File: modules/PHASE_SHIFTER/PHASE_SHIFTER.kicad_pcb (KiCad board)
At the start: 2 copper layers, 160 x 100 mm, 2 parts, among them J1 Card_Connector

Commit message: started phase shifter
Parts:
- added C1: 470n, FormantKO:C_Rect, F.Cu at (123.2, 101.2)
- added C10: 10µ, FormantKO:CP_Axial_600, F.Cu at (182.0, 110.0)
- added C11: 10µ, FormantKO:CP_Axial_600, F.Cu at (182.0, 80.0)
- added C2: 4µ7, FormantKO:CP_Axial_600, F.Cu at (139.6, 121.7)
- added C3: 1µ, FormantKO:C_Rect, F.Cu at (123.2, 105.3)
- added C4: 470n, FormantKO:C_Rect, F.Cu at (123.2, 109.4)
- added C5: 330n, FormantKO:C_Rect, F.Cu at (123.2, 113.5)
- added C6: 150n, FormantKO:C_Rect, F.Cu at (123.2, 117.6)
- added C7: 100n, FormantKO:C_Rect, F.Cu at (123.2, 121.7)
- added C8: 47n, FormantKO:C_Rect, F.Cu at (123.2, 125.8)
- added D1: type="" model="12V" lib="semiconductor.lib", FormantKO:DUZ, F.Cu at (189.0, 111.9)
- added D2: 12V, FormantKO:DUZ, F.Cu at (189.0, 82.0)
- added IC1: LM324, FormantKO:DIP-14, F.Cu at (136.1, 108.8)
- added IC2: LM324, FormantKO:DIP-14, F.Cu at (147.7, 108.8)
- added P2: 50k, FormantKO:Potentiometer_Trimmer, F.Cu at (159.0, 120.3)
- added P4: 10k, FormantKO:PanelConnector_1x03, F.Cu at (159.5, 102.5)
- added R1: 100k, FormantKO:R_Axial_Horizontal, F.Cu at (126.5, 64.8)
- added R10: 22k, FormantKO:R_Axial_Horizontal, F.Cu at (142.3, 64.8)
- added R11: 22k, FormantKO:R_Axial_Horizontal, F.Cu at (142.3, 68.8)
- added R12: 22k, FormantKO:R_Axial_Horizontal, F.Cu at (142.3, 72.8)
- added R13: 22k, FormantKO:R_Axial_Horizontal, F.Cu at (142.3, 76.9)
- added R14: 22k, FormantKO:R_Axial_Horizontal, F.Cu at (142.3, 81.0)
- added R15: 100k, FormantKO:R_Axial_Horizontal, F.Cu at (142.3, 85.0)
- added R16: 100k, FormantKO:R_Axial_Horizontal, F.Cu at (142.3, 89.0)
- added R17: 100k, FormantKO:R_Axial_Horizontal, F.Cu at (142.3, 93.1)
- added R18: 100k, FormantKO:R_Axial_Horizontal, F.Cu at (142.3, 97.2)
- added R19: 100k, FormantKO:R_Axial_Horizontal, F.Cu at (158.1, 64.8)
- added R2: 100k, FormantKO:R_Axial_Horizontal, F.Cu at (126.5, 68.8)
- added R20: 100k, FormantKO:R_Axial_Horizontal, F.Cu at (158.1, 68.8)
- added R21: 22k, FormantKO:R_Axial_Horizontal, F.Cu at (158.1, 72.8)
- added R22: 22k, FormantKO:R_Axial_Horizontal, F.Cu at (158.1, 76.9)
- added R23: 10k, FormantKO:R_Axial_Horizontal, F.Cu at (158.1, 81.0)
- added R3: 22k, FormantKO:R_Axial_Horizontal, F.Cu at (126.5, 72.8)
- added R35: 10k, FormantKO:R_Axial_Horizontal, F.Cu at (158.1, 85.0)
- added R37: 150R, FormantKO:R_Axial_Horizontal, F.Cu at (195.0, 111.3)
- added R38: 150R, FormantKO:R_Axial_Horizontal, F.Cu at (195.0, 78.7)
- added R4: 22k, FormantKO:R_Axial_Horizontal, F.Cu at (126.5, 76.9)
- added R5: 22k, FormantKO:R_Axial_Horizontal, F.Cu at (126.5, 81.0)
- added R6: 22k, FormantKO:R_Axial_Horizontal, F.Cu at (126.5, 85.0)
- added R7: 22k, FormantKO:R_Axial_Horizontal, F.Cu at (126.5, 89.0)
- added R8: 22k, FormantKO:R_Axial_Horizontal, F.Cu at (126.5, 93.1)
- added R9: 22k, FormantKO:R_Axial_Horizontal, F.Cu at (126.5, 97.2)
- added S1: PHASING, FormantKO:PanelConnector_1x03, F.Cu at (159.5, 110.3)
- added T1: N-FET, FormantKO:TO-92, F.Cu at (112.0, 66.8)
- added T2: N-FET, FormantKO:TO-92, F.Cu at (112.0, 73.4)
- added T3: N-FET, FormantKO:TO-92, F.Cu at (112.0, 80.0)
- added T4: N-FET, FormantKO:TO-92, F.Cu at (112.0, 86.6)
- added T5: N-FET, FormantKO:TO-92, F.Cu at (112.0, 93.2)
- added T6: N-FET, FormantKO:TO-92, F.Cu at (112.0, 99.8)
- MH1: value ~ -> CardBracket; footprint FormantKO:Schroff_60807-011_3U_Pair -> FormantKO:Card_Bracket
- moved MH1 50.0 mm to (55.0, 95.0)
- moved J1 40.2 mm to (215.0, 95.0)

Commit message: not sure
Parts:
- moved P2 110.3 mm to (63.9, 64.5)
- moved S1 102.8 mm to (61.3, 79.8), turned to -90 degrees
- moved P4 98.2 mm to (61.3, 100.1), turned to -90 degrees
- moved R20 93.0 mm to (71.5, 102.6), turned to 90 degrees
- moved R22 84.7 mm to (74.0, 87.4)
- moved R23 84.5 mm to (74.0, 72.1), turned to 90 degrees
- moved R21 79.0 mm to (79.1, 72.1), turned to 90 degrees
- moved C2 76.5 mm to (74.0, 82.3)
- moved R35 74.8 mm to (96.9, 128.0), turned to 90 degrees
- moved T1 72.4 mm to (168.0, 112.8), turned to -90 degrees
- moved R14 66.3 mm to (81.7, 107.7)
- moved R13 65.9 mm to (81.7, 102.6)
- moved IC2 65.3 mm to (89.3, 79.8), turned to 180 degrees
- moved R19 61.5 mm to (104.5, 95.0)
- moved T2 60.4 mm to (157.9, 112.8), turned to -90 degrees
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
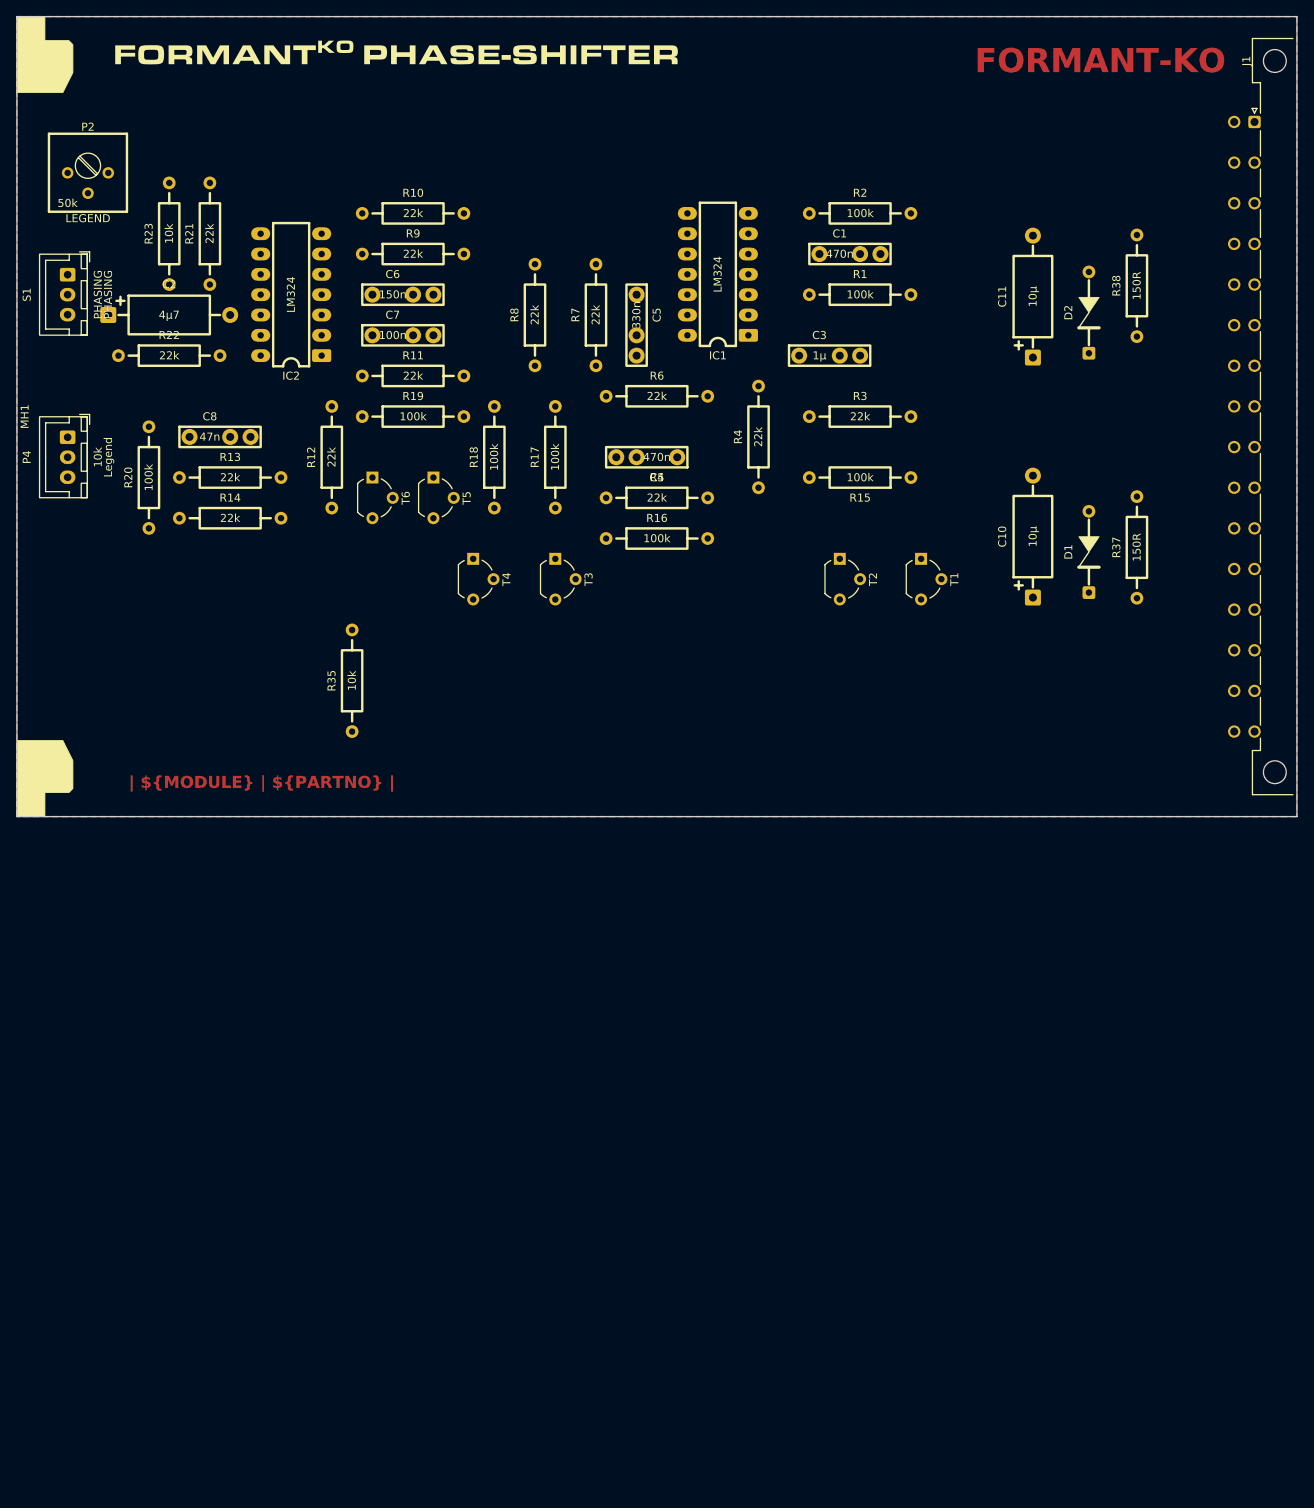
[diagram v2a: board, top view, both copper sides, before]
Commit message: phase shifter pcb placement
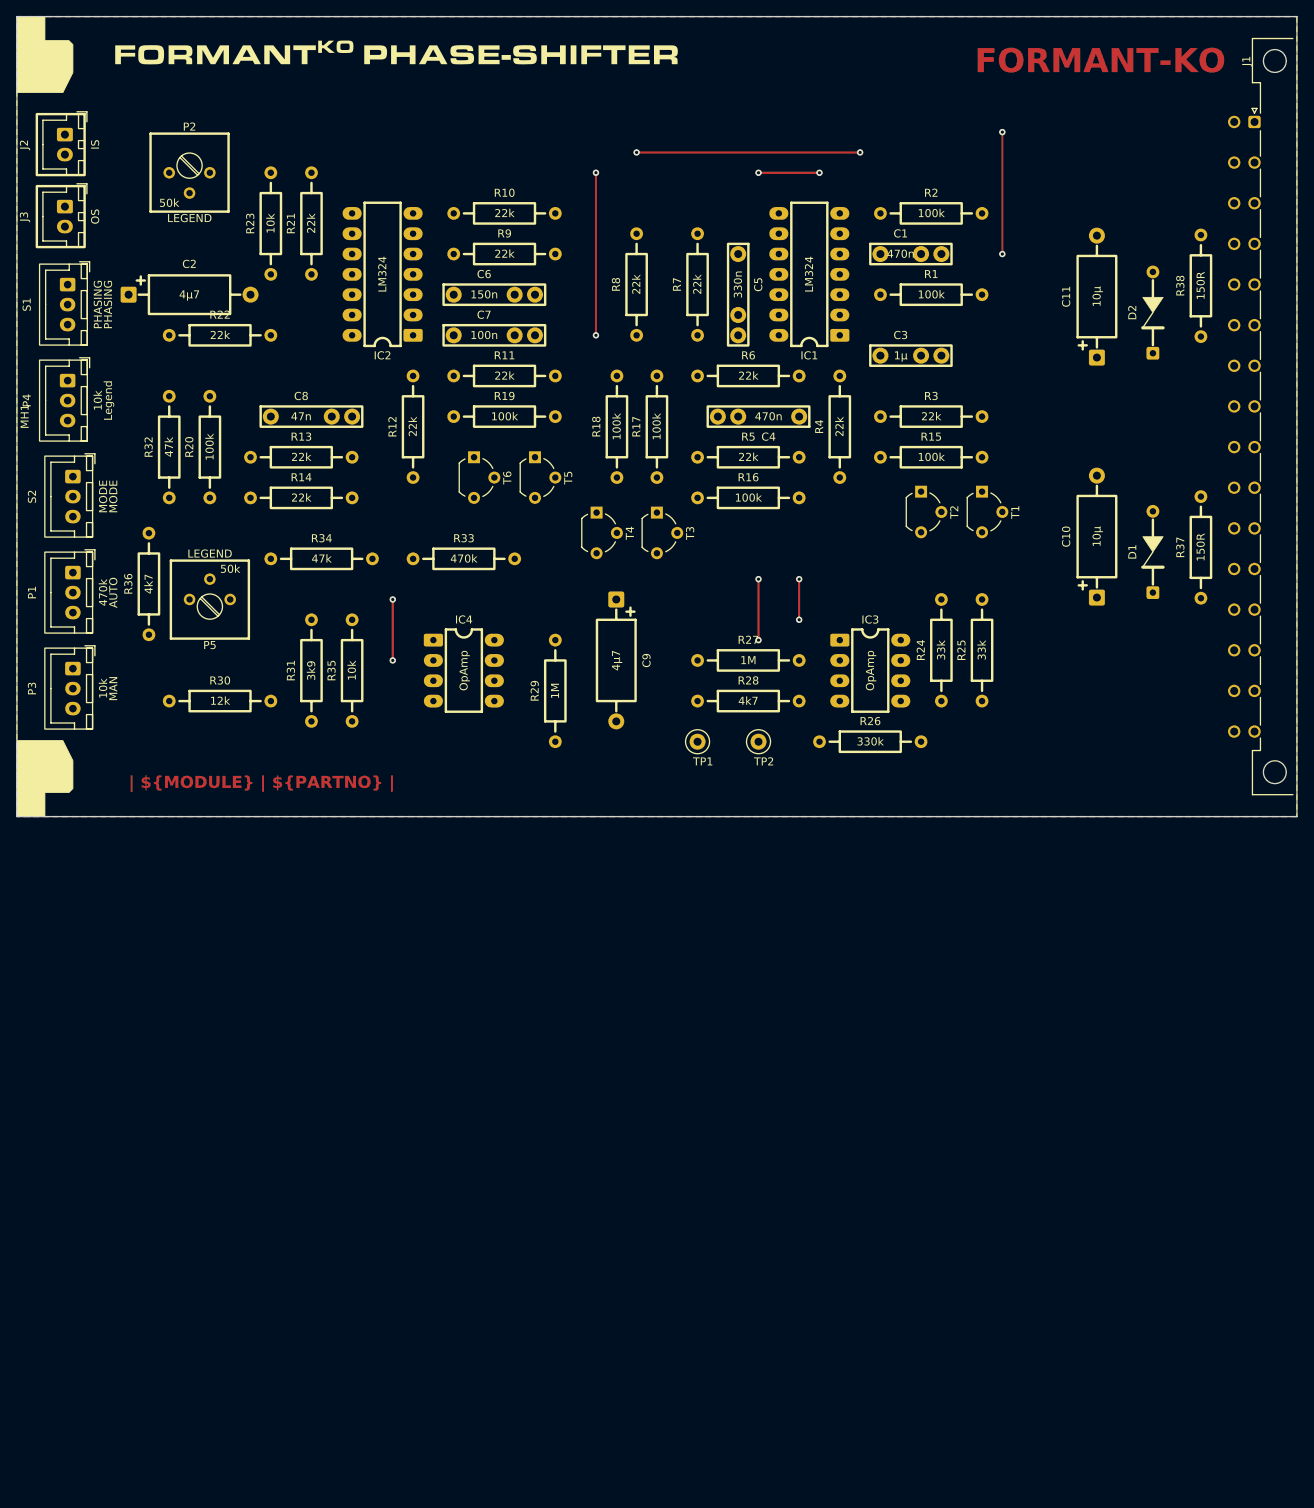
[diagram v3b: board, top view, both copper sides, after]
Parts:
- added C9: 4µ7, FormantKO:CP_Axial_600, F.Cu at (129.9, 125.5)
- added IC3: OpAmp, FormantKO:DIP-8, F.Cu at (161.7, 126.8)
- added IC4: OpAmp, FormantKO:DIP-8, F.Cu at (110.9, 126.8)
- added J2: IS, FormantKO:PanelConnector_1x02, F.Cu at (61.0, 61.0)
- added J3: OS, FormantKO:PanelConnector_1x02, F.Cu at (61.0, 70.0)
- added P1: 470k, FormantKO:PanelConnector_1x03, F.Cu at (62.0, 117.0)
- added P3: 10k, FormantKO:PanelConnector_1x03, F.Cu at (62.0, 129.0)
- added P5: 50k, FormantKO:Potentiometer_Trimmer, F.Cu at (79.1, 117.9)
- added R24: 33k, FormantKO:R_Axial_Horizontal, F.Cu at (170.6, 124.2)
- added R25: 33k, FormantKO:R_Axial_Horizontal, F.Cu at (175.6, 124.2)
- added R26: 330k, FormantKO:R_Axial_Horizontal, F.Cu at (161.7, 135.6)
- added R27: 1M, FormantKO:R_Axial_Horizontal, F.Cu at (146.4, 125.5)
- added R28: 4k7, FormantKO:R_Axial_Horizontal, F.Cu at (146.4, 130.6)
- added R29: 1M, FormantKO:R_Axial_Horizontal, F.Cu at (122.3, 129.3)
- added R30: 12k, FormantKO:R_Axial_Horizontal, F.Cu at (80.4, 130.6)
- added R31: 3k9, FormantKO:R_Axial_Horizontal, F.Cu at (91.8, 126.8)
- added R32: 47k, FormantKO:R_Axial_Horizontal, F.Cu at (74.0, 98.8)
- added R33: 470k, FormantKO:R_Axial_Horizontal, F.Cu at (110.9, 112.8)
- added R34: 47k, FormantKO:R_Axial_Horizontal, F.Cu at (93.1, 112.8)
- added R36: 4k7, FormantKO:R_Axial_Horizontal, F.Cu at (71.5, 115.9)
- added S2: MODE, FormantKO:PanelConnector_1x03, F.Cu at (62.0, 105.0)
- added TP1: SQUARE, TestPoint:TestPoint_Loop_D2.50mm_Drill1.0mm, F.Cu at (140.1, 135.6)
- added TP2: TRIANGLE, TestPoint:TestPoint_Loop_D2.50mm_Drill1.0mm, F.Cu at (147.7, 135.6)
- C4, C5, C6, C7, C8: footprint FormantKO:C_Rect -> FormantKO:C_Rect_300_400
- D1: value type="" model="12V" lib="semiconductor.lib" -> 12V
- J1: footprint FormantKO:Card_Connector -> FormantKO:CardConnector
- MH1: footprint FormantKO:Card_Bracket -> FormantKO:CardBracket
- moved T4 16.5 mm to (127.5, 107.0)
- moved R18 15.8 mm to (130.0, 96.3)
- moved C4 14.9 mm to (149.0, 95.0)
- moved T3 14.0 mm to (135.0, 107.0)
- moved R7 13.3 mm to (140.1, 78.5)
- moved R17 13.3 mm to (135.0, 96.3)
- moved R8 13.3 mm to (132.5, 78.5)
- moved C5 13.3 mm to (145.2, 78.5)
- moved T2 13.2 mm to (168.0, 104.4)
- moved T5 13.0 mm to (119.8, 100.1)
- moved T6 13.0 mm to (112.1, 100.1)
- moved R21 12.8 mm to (91.8, 70.9)
- moved R23 12.8 mm to (86.7, 70.9)
- moved P2 12.7 mm to (76.6, 64.5)
- moved R16 12.5 mm to (146.4, 105.2)
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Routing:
- net (no net): track 0.00 -> 91.4 mm, vias 0 -> 14

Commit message: phase shifter trace work
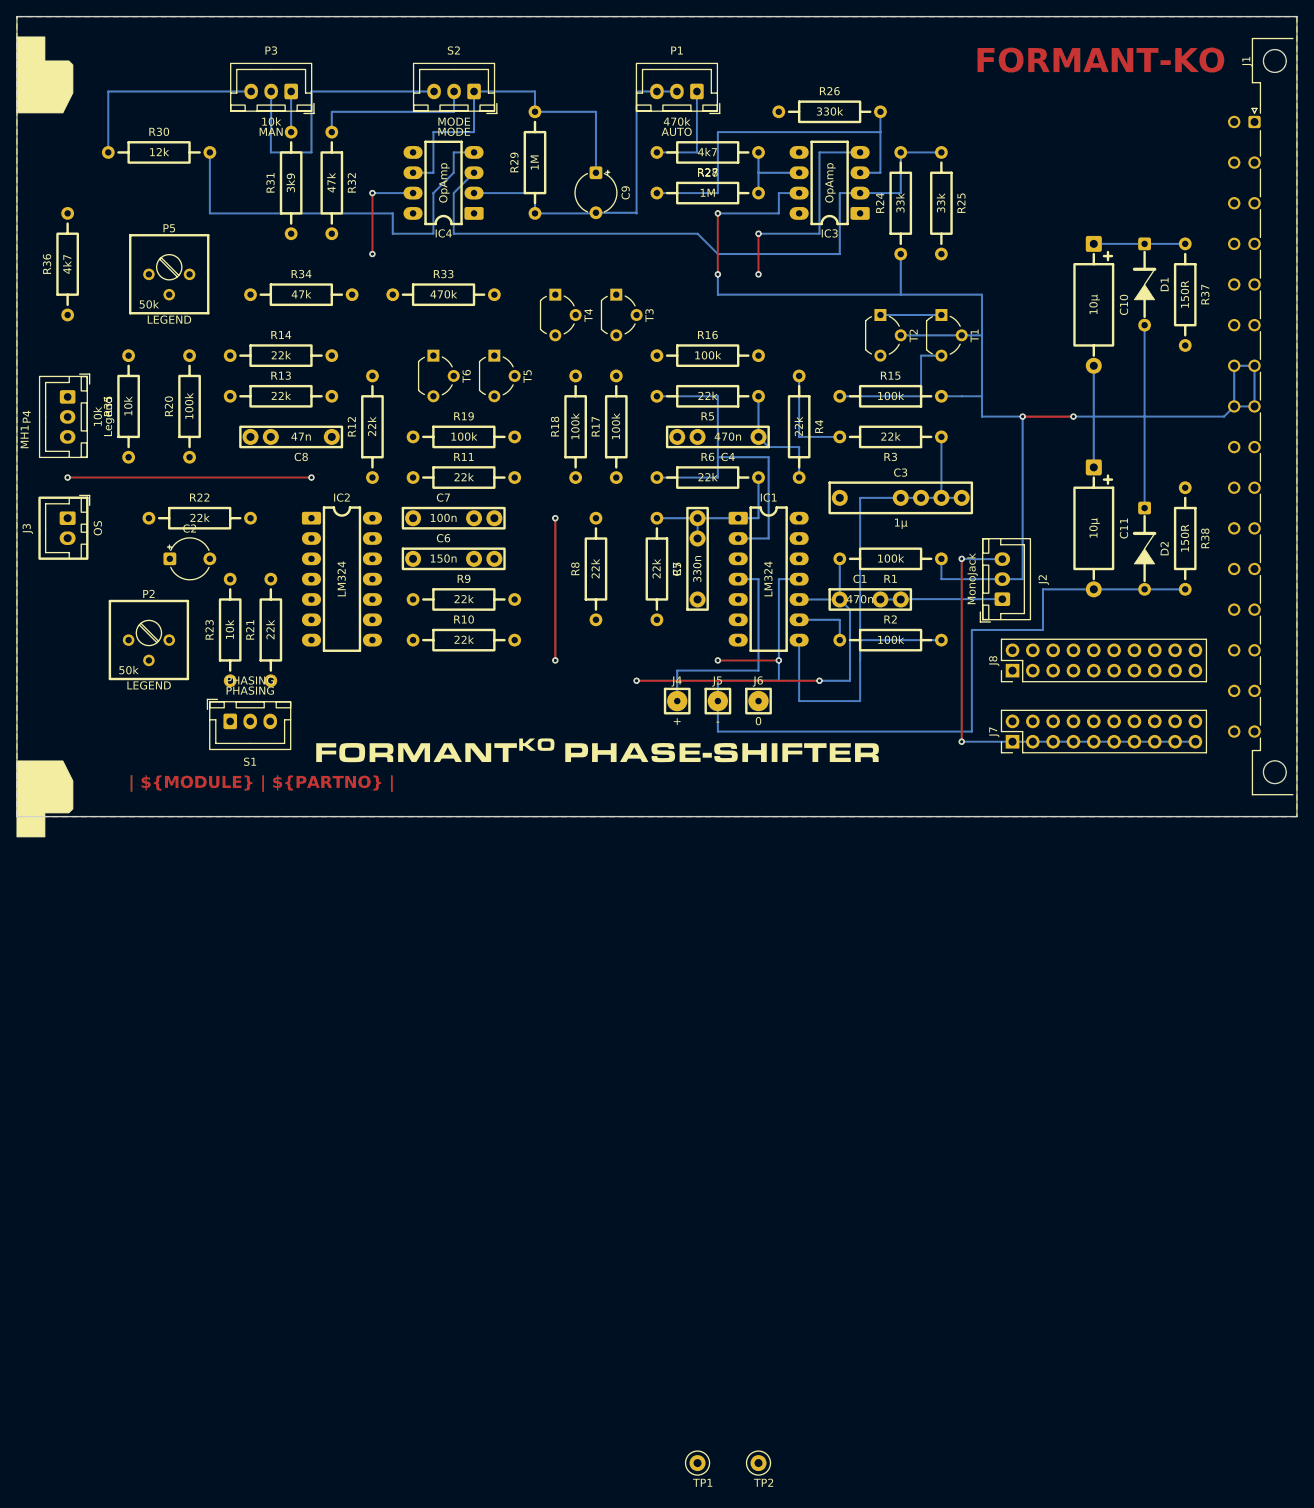
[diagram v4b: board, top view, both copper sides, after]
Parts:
- added J4: +, FormantKO:Wire_1x01_General, F.Cu at (137.5, 130.6)
- added J5: -, FormantKO:Wire_1x01_General, F.Cu at (142.6, 130.6)
- added J6: 0, FormantKO:Wire_1x01_General, F.Cu at (147.7, 130.6)
- added J7: IS SELECT, Connector_PinHeader_2.54mm:PinHeader_2x10_P2.54mm_Vertical, F.Cu at (179.4, 135.6)
- added J8: OS SELECT, Connector_PinHeader_2.54mm:PinHeader_2x10_P2.54mm_Vertical, F.Cu at (179.4, 126.8)
- C2, C9: footprint FormantKO:CP_Axial_600 -> Capacitor_THT:CP_Radial_Tantal_D5.0mm_P5.00mm
- C3: footprint FormantKO:C_Rect -> FormantKO:C_Rect_300_400_500_600
- J2: value IS -> MonoJack; footprint FormantKO:PanelConnector_1x02 -> FormantKO:PanelConnector_1x03
- moved J2 129.2 mm to (178.2, 115.3), turned to 90 degrees
- moved P1 98.1 mm to (137.5, 54.4), turned to 180 degrees
- moved TP1 90.2 mm to (140.1, 225.8)
- moved TP2 90.2 mm to (147.7, 225.8)
- moved R26 78.9 mm to (156.6, 56.9)
- moved P3 78.6 mm to (86.8, 54.4), turned to 180 degrees
- moved S2 69.5 mm to (109.6, 54.4), turned to 180 degrees
- moved R30 69.0 mm to (72.8, 62.0)
- moved R28 68.8 mm to (141.3, 62.0), turned to 180 degrees
- moved R29 66.1 mm to (119.8, 63.2)
- moved IC3 61.2 mm to (156.6, 65.8), turned to 180 degrees
- moved C9 61.0 mm to (127.4, 64.5)
- moved IC4 61.0 mm to (108.3, 65.8), turned to 180 degrees
- moved R31 61.0 mm to (89.3, 65.8)
- moved P2 58.6 mm to (71.5, 122.9)
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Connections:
- C1 pad 1: IS -> Net-(IC1C-+)
- C1 pad 2: Net-(IC1C-+) -> ES
- C3 pad 1: Net-(C3-Pad1) -> Net-(IC1D-+)
- C3 pad 2: Net-(IC1D-+) -> Net-(C3-Pad2)
- C5 pad 1: Net-(C5-Pad1) -> Net-(IC1B-+)
- C5 pad 2: Net-(IC1B-+) -> Net-(C5-Pad2)
- IC1 pad 1: Net-(C5-Pad1) -> Net-(C5-Pad2)
- IC1 pad 8: Net-(C3-Pad1) -> Net-(C3-Pad2)
- J1 pad a24: unconnected-(J1-VCO1-Pada24) -> VCO1
- J1 pad a26: unconnected-(J1-VCO3-Pada26) -> VCO3
- J1 pad a28: unconnected-(J1-VCF1-Pada28) -> VCF1
- J1 pad a30: unconnected-(J1-VCA1-Pada30) -> VCA1
- J1 pad a32: unconnected-(J1-COM1-Pada32) -> COM1
- J1 pad b24: unconnected-(J1-VCO2-Padb24) -> VCO2
- J1 pad b26: unconnected-(J1-RFM-Padb26) -> RFM
- J1 pad b28: unconnected-(J1-VCF2-Padb28) -> VCF2
- J1 pad b30: unconnected-(J1-VCA2-Padb30) -> VCA2
- J1 pad b32: unconnected-(J1-PA1-Padb32) -> PA1
- J2 pad 1: GND -> ES
- J2 pad 2: IS -> GND
- R2 pad 2: Net-(C3-Pad1) -> Net-(C3-Pad2)
- R3 pad 1: Net-(C3-Pad1) -> Net-(C3-Pad2)
- R6 pad 2: Net-(C5-Pad1) -> Net-(C5-Pad2)
- R7 pad 1: Net-(C5-Pad1) -> Net-(C5-Pad2)
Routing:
- net GND: track 0.00 -> 250.5 mm, vias 0 -> 8
- net -12V: track 0.00 -> 192.8 mm, vias 0 -> 4
- net Net-(IC3--): track 0.00 -> 83.4 mm
- net (no net): track 91.4 -> 17.8 mm, vias 14 -> 2
- net Net-(C3-Pad2): track 0.00 -> 73.7 mm
- net IS: track 0.00 -> 57.2 mm, vias 0 -> 2
- net Net-(IC1C-+): track 0.00 -> 47.5 mm, vias 0 -> 2
- net Net-(IC1A--): track 0.00 -> 45.7 mm
- net Net-(IC3-+): track 0.00 -> 45.7 mm
- net Net-(IC4--): track 0.00 -> 43.2 mm
- net Net-(S2-a): track 0.00 -> 43.2 mm
- net +12V: track 0.00 -> 39.4 mm
- net Net-(S2-b): track 0.00 -> 35.7 mm
- net Net-(P3-Pad3): track 0.00 -> 25.5 mm
- net Net-(S2-c): track 0.00 -> 20.3 mm
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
